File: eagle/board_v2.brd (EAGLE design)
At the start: 100 x 62.9 mm, 35 parts, among them J1 RJ11-4X, J2 RJ11-4X, Q1 BD140, Q10 BD140, Q11 BD140, Q12 BD140, Q13 BD140, Q14 BD140, Q15 BD140, Q2 BD140, Q3 BD140, Q4 BD140, Q5 BD140, Q6 BD140, Q7 BD140, Q8 BD140, Q9 BD140, X1 RJ45-8X, X2 RJ45-8X, X3 RJ45-8X, X4 RJ45-8X, X5 RJ45-8X, X6 RJ45-8X

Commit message: board v2.2
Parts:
- removed S1: (no value), switch-dil:DS-04
- removed X1, X2, X3, X4, X5: RJ45-8X, con-tycoelectronics:RJ45-NO-SHIELD
- added C3: 1u, resistor:C1206
- added JP1: (no value), pinhead:2X04
- added PWR: ARK210/2EX, con-brm:ARK210/2EX
- added X10, X7, X8, X9: 22-23-2041, con-molex:22-23-2041
- C2: device resistor:PANASONIC_C -> resistor:E2,5-5
- R4: value 10k -> 4k7
- X6: value RJ45-8X -> 22-23-2041; device con-tycoelectronics:RJ45-NO-SHIELD -> con-molex:22-23-2041
- moved Q9 74.4 mm to (19.7, 11.4), turned to 90 degrees
- moved Q8 68.4 mm to (23.5, 11.4), turned to 90 degrees
- moved X6 63.6 mm to (3.81, 43.8), turned to 90 degrees
- moved Q7 62.3 mm to (27.3, 11.4), turned to 90 degrees
- moved J2 49.0 mm to (44.1, 25.7), turned to 90 degrees
- moved Q12 48.7 mm to (37.5, 11.4), turned to 90 degrees
- moved Q4 46.8 mm to (11.4, 12.7)
- moved J1 45.7 mm to (44.1, 41.6), turned to 90 degrees
- moved Q11 42.9 mm to (41.3, 11.4), turned to 90 degrees
- moved Q3 41.3 mm to (11.4, 48.9)
- moved R5 38.8 mm to (18.4, 46.4), turned to 180 degrees
- moved Q5 38.2 mm to (11.4, 16.5)
- moved Q10 37.3 mm to (45.1, 11.4), turned to 90 degrees
- moved R6 34.6 mm to (18.4, 43.8), turned to 180 degrees
- moved Q2 32.7 mm to (11.4, 45.1)
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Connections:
- net +5V: now also C3.1, PWR.P$1, X10.2, X7.2, X8.2, X9.2; no longer X1.4, X2.4, X3.4, X4.4, X5.4, X6.1, X6.3, X6.4
- net GND: now also C3.2, JP1.1, JP1.3, JP1.5, JP1.7, PWR.P$2; no longer S1.5, S1.6, S1.7, S1.8, X6.5, X6.6, X6.7, X6.8
- net N$1: now also X6.1; no longer X1.2
- net N$10: now also X10.1; no longer X4.2
- net N$11: now also X10.3; no longer X4.6
- net N$12: now also X10.4; no longer X4.8
- net N$13: now also X7.1; no longer X5.2
- net N$14: now also X7.3; no longer X5.6
- net N$15: now also X7.4; no longer X5.8
- net N$17: now also JP1.2; no longer S1.4
- net N$18: now also JP1.4; no longer S1.3
- net N$19: now also JP1.6; no longer S1.2
- net N$2: now also X6.3; no longer X1.6
- net N$20: now also JP1.8; no longer S1.1
- net N$3: now also X6.4; no longer X1.8
- net N$4: now also X8.1; no longer X2.2
- net N$5: now also X8.3; no longer X2.6
- net N$6: now also X8.4; no longer X2.8
- net N$7: now also X9.1; no longer X3.2
- net N$8: now also X9.3; no longer X3.6
- net N$9: now also X9.4; no longer X3.8
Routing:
- net +5V: track 312.3 -> 167.3 mm, vias 4 -> 3
- net N$37: track 103.6 -> 28.5 mm, vias 0 -> 1
- net N$38: track 73.2 -> 36.8 mm
- net N$22: track 49.9 -> 24.8 mm
- net N$23: track 46.2 -> 21.8 mm
- net N$24: track 41.6 -> 18.8 mm
- net N$16: track 35.1 -> 12.7 mm
- net N$25: track 30.2 -> 10.1 mm
- net N$26: track 25.8 -> 8.82 mm
- net N$30: track 30.2 -> 14.2 mm
- net N$20: track 44.0 -> 29.0 mm, vias 0 -> 1
- net N$19: track 39.7 -> 25.2 mm, vias 0 -> 1
- net N$31: track 28.4 -> 14.0 mm
- net N$18: track 35.4 -> 21.3 mm, vias 0 -> 1
- net N$32: track 26.5 -> 12.8 mm
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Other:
- board size 100 x 62.9 mm -> 49.5 x 49.5 mm
- board text removed: "C1"
- board text removed: "C2"
- board text removed: "J1"
- board text removed: "J2"
- board text removed: "Q1"
- board text removed: "Q10"
- board text removed: "Q11"
- board text removed: "Q12"
- board text removed: "Q13"
- board text removed: "Q14"
- board text removed: "Q15"
- board text removed: "Q2"
- board text removed: "Q3"
- board text removed: "Q4"
- board text removed: "Q5"
- board text removed: "Q6"
- board text removed: "Q7"
- board text removed: "Q8"
- board text removed: "Q9"
- board text removed: "R1"
- board text removed: "R2"
- board text removed: "R3"
- board text removed: "R4"
- board text removed: "R5"
- board text removed: "R6"
- board text removed: "R7"
- board text removed: "R8"
- board text removed: "S1"
- board text removed: "U$1"
- board text removed: "X2"
- board text removed: "X3"
- board text removed: "X4"
- board text removed: "X6"
- board text removed: "brmlab"
- board text removed: "ledbar v2.1"

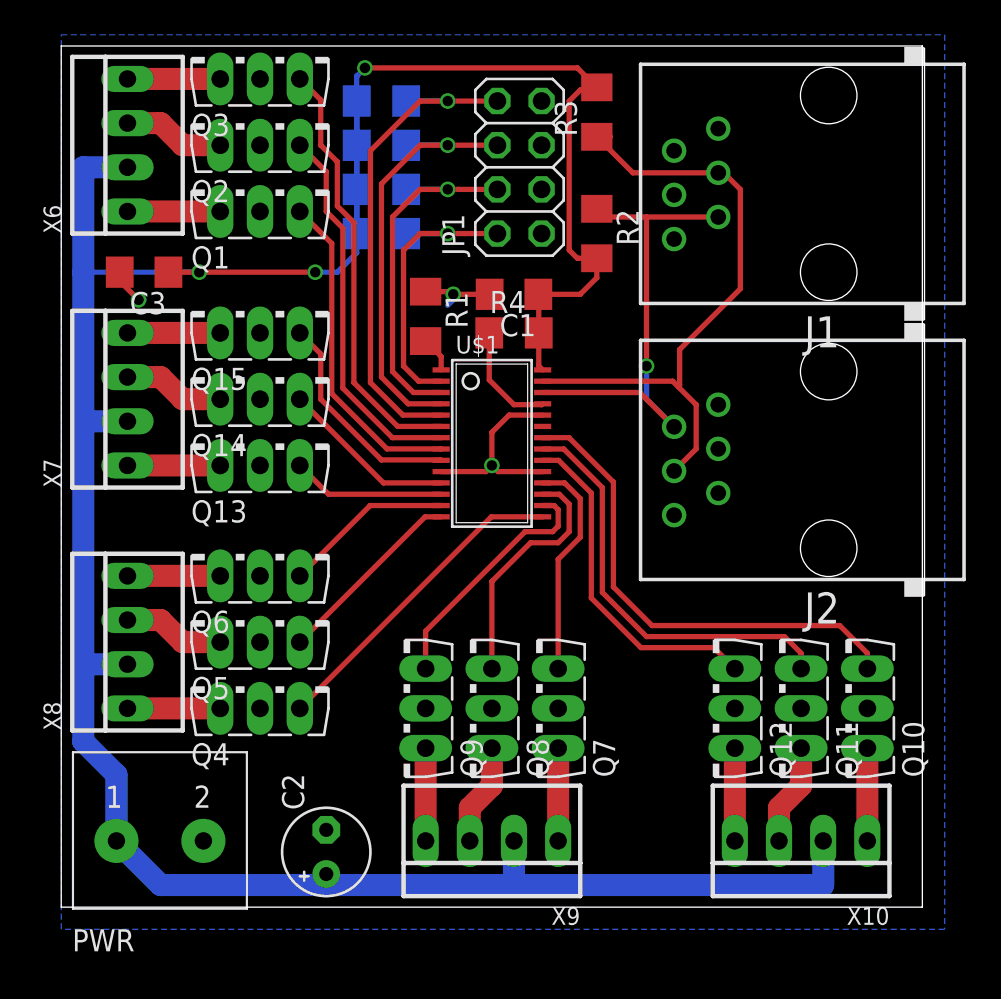
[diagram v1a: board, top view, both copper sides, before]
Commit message: board v2.2 - silkscreen cleanup
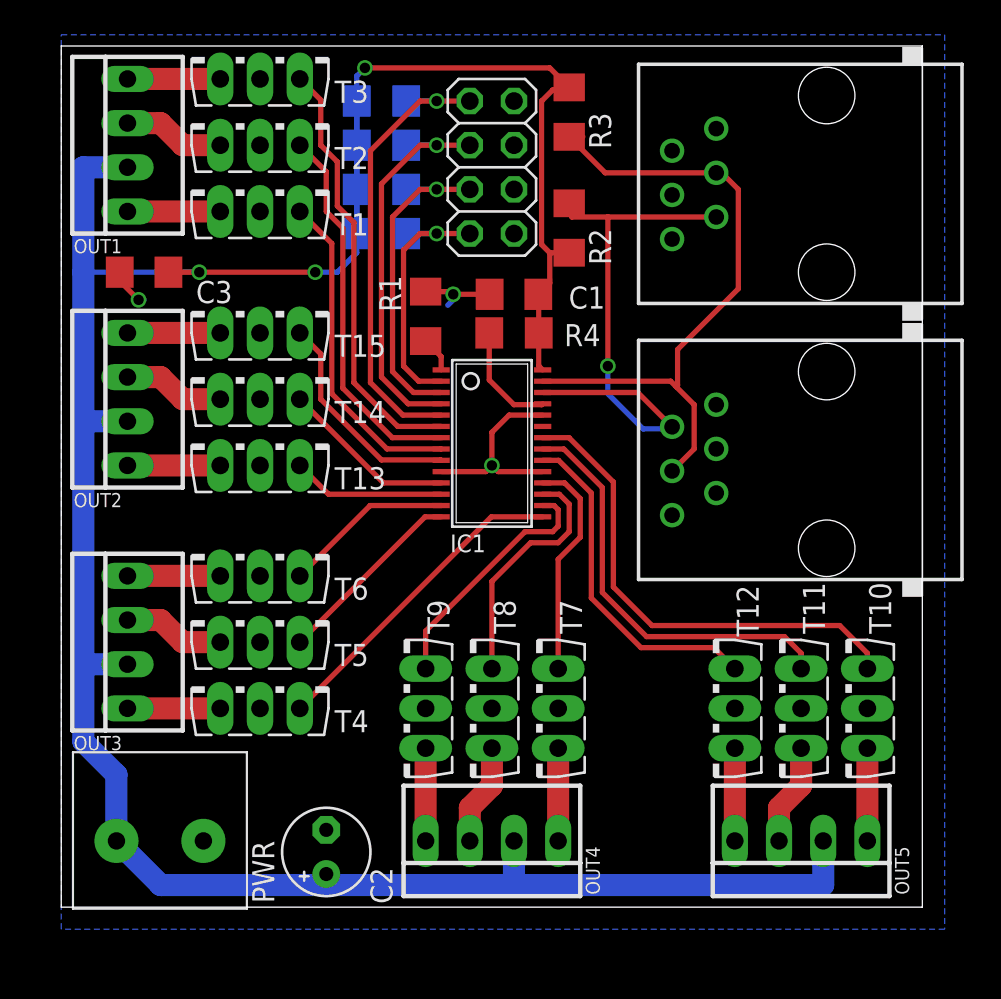
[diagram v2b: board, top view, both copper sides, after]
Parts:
- removed J1, J2: RJ11-4X, con-tycoelectronics:RJ11-NO_SHIELD
- added I2C-IN, I2C-OUT: RJ11-4X, con-tycoelectronics:RJ11-NO_SHIELD
- moved R2 1.62 mm to (29.2, 39.1)
- moved JP1 1.59 mm to (24.8, 42.5)
- moved R3 1.59 mm to (29.2, 45.7)
- renumbered Q1 to T1, Q10 to T10, Q11 to T11, Q12 to T12, Q13 to T13, Q14 to T14, Q15 to T15, Q2 to T2, Q3 to T3, Q4 to T4, Q5 to T5, Q6 to T6, Q7 to T7, Q8 to T8, Q9 to T9, U$1 to IC1, X10 to OUT5, X6 to OUT1, X7 to OUT2, X8 to OUT3, X9 to OUT4
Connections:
- net GND: now also I2C-IN.3, I2C-IN.5, I2C-OUT.2, I2C-OUT.4; no longer J1.3, J1.5, J2.2, J2.4
- net N$37: now also I2C-IN.2, I2C-OUT.5; no longer J1.2, J2.5
- net N$38: now also I2C-IN.4, I2C-OUT.3; no longer J1.4, J2.3
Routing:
- net +5V: track 167.3 -> 163.2 mm
- net N$37: track 28.5 -> 32.6 mm
- net N$18: track 21.3 -> 19.0 mm
- net N$17: track 17.4 -> 15.1 mm
- net N$20: track 29.0 -> 26.8 mm
- net N$19: track 25.2 -> 23.3 mm
- net N$38: track 36.8 -> 38.2 mm
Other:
- board text added: "+"
- board text added: "-"
- board text added: "/home/nephirus/brmlab.bmp"
- board text added: "0"
- board text added: "1"
- board text added: "2"
- board text added: "3"

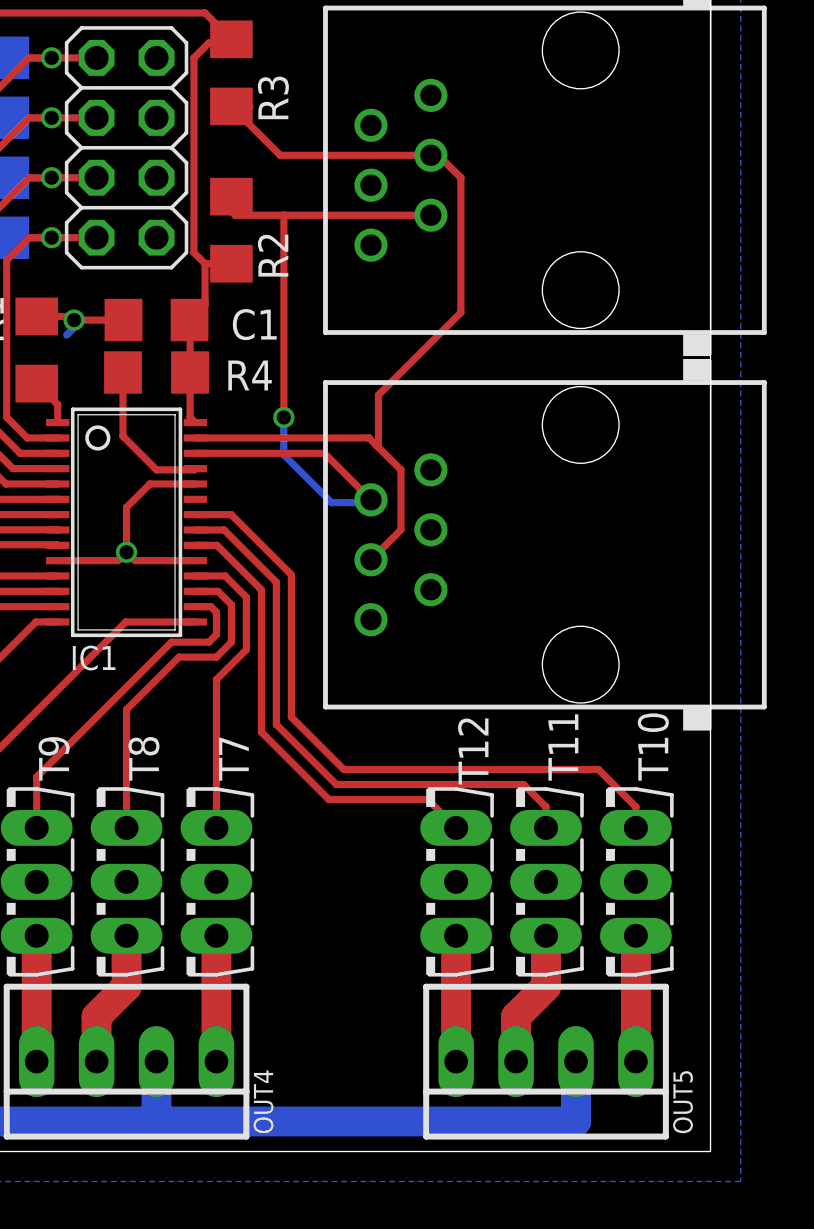
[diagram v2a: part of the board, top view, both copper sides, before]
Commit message: Board v2.2 - power-on LED added; minor adjustments to silkscreen (version, brmlab logo)
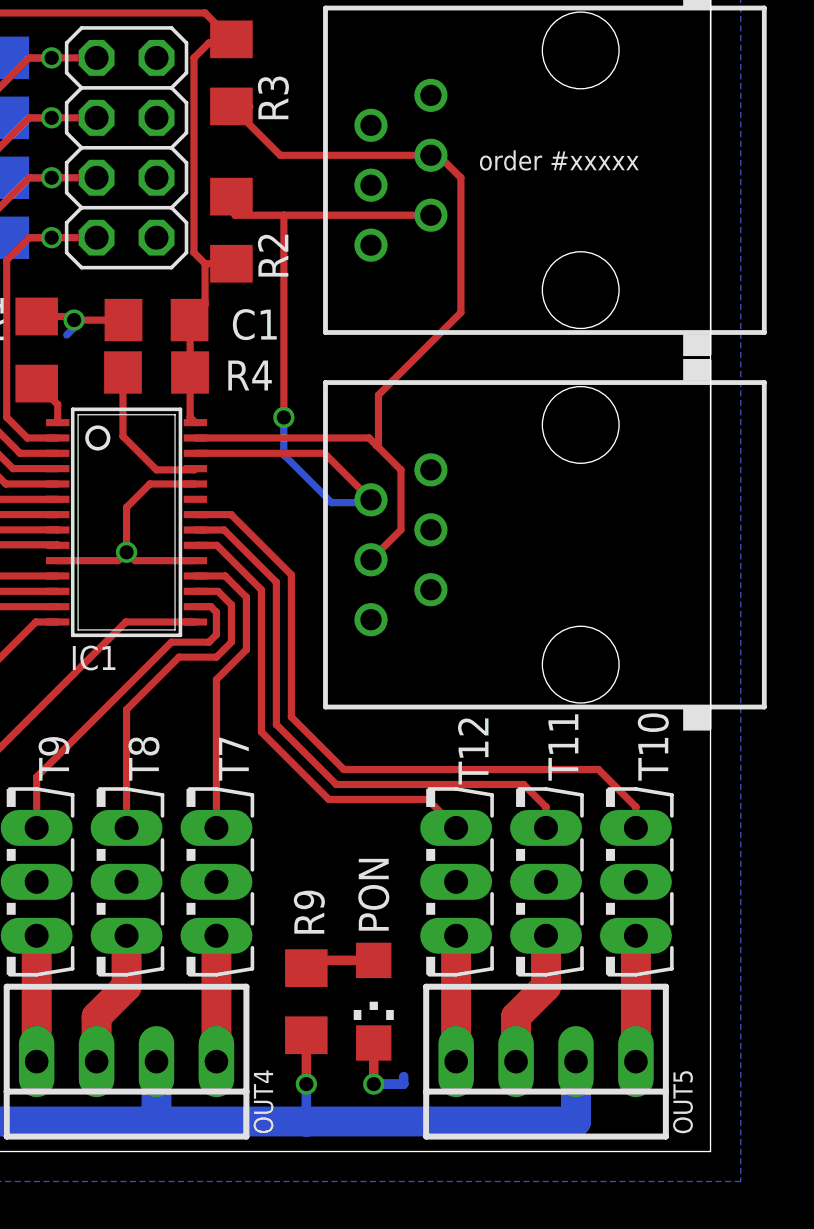
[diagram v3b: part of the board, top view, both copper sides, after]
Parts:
- added PON: (no value), led:CHIPLED_1206
- added R9: 220R, resistor:R1206
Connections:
- new net N$39: PON.A, R9.2
- net +5V: now also R9.1
- net GND: now also PON.C
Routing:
- net +5V: track 163.2 -> 166.8 mm, vias 3 -> 4
- net GND: track 18.5 -> 21.9 mm, vias 3 -> 4
- net N$39: track 0.00 -> 3.19 mm
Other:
- board text added: "ledbar v2.2"
- board text added: "order #xxxxx"
